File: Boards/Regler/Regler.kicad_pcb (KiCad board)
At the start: 2 copper layers, 21 parts, among them P1 CONN_2, P2 CONN_3, P3 CONN_3, P4 CONN_3, P5 CONN_3, P6 CONN_3, SW1 SP3T

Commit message: Anoden-Stabi auf eigenes Board, Endstufe Layouttest
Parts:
- RL1, RL2, RL3: footprint w_relay:relay_40.52 -> Relays_ThroughHole:Relay_DPDT_Schrack-RT2_RM5mm
- moved P6 54.8 mm to (130.0, 94.5)
- moved RL1 46.0 mm to (183.4, 113.3)
- moved D1 41.4 mm to (179.8, 120.4)
- moved P2 34.5 mm to (195.1, 94.5)
- moved RL2 29.8 mm to (148.8, 113.3)
- moved D6 27.9 mm to (195.6, 137.7)
- moved R3 27.0 mm to (198.1, 126.5), turned to 270 degrees
- moved D3 23.5 mm to (144.8, 120.4), turned to 180 degrees
- moved D2 18.2 mm to (215.4, 137.7)
- moved RL3 18.1 mm to (118.4, 113.8)
- moved R2 13.5 mm to (208.8, 126.5), turned to 270 degrees
- moved D4 12.2 mm to (206.2, 137.7)
- moved D5 11.4 mm to (114.8, 120.4), turned to 180 degrees
- moved P3 11.0 mm to (162.6, 94.5)
- moved RV1 10.8 mm to (83.3, 137.2)
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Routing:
- net Earth_Clean: track 25.0 -> 188.3 mm
- net Net-(P3-Pad1): track 136.3 -> 22.4 mm
- net +12V: track 85.8 -> 0.00 mm
- net Net-(P6-Pad1): track 79.1 -> 20.6 mm
- net Net-(D1-Pad1): track 137.1 -> 82.0 mm
- net Net-(RL1-Pad24): track 47.3 -> 0.00 mm
- net Net-(D5-Pad1): track 203.8 -> 159.2 mm
- net Net-(RL1-Pad14): track 41.0 -> 0.00 mm
- net GND: track 0.00 -> 36.1 mm
- net Net-(P6-Pad3): track 41.4 -> 13.8 mm
- net Net-(D3-Pad1): track 141.3 -> 117.4 mm
- net Net-(P2-Pad3): track 28.3 -> 14.0 mm
- net Net-(P3-Pad3): track 29.8 -> 16.1 mm
- net Net-(D6-Pad2): track 3.81 -> 6.10 mm
- net Net-(D4-Pad2): track 3.81 -> 6.10 mm
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- added copper zone on B.Cu, net GND
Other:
- net class Default: trace_width 0.5 -> 1

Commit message: Work in Progress
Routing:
- net Net-(RL1-Pad24): track 0.00 -> 69.7 mm
- net Net-(RL1-Pad14): track 0.00 -> 69.7 mm
- net +12V: track 0.00 -> 49.4 mm, vias 0 -> 2
- net Net-(D3-Pad1): track 117.4 -> 122.6 mm
- net Earth_Clean: track 188.3 -> 186.8 mm
- net Net-(D1-Pad1): track 82.0 -> 80.5 mm

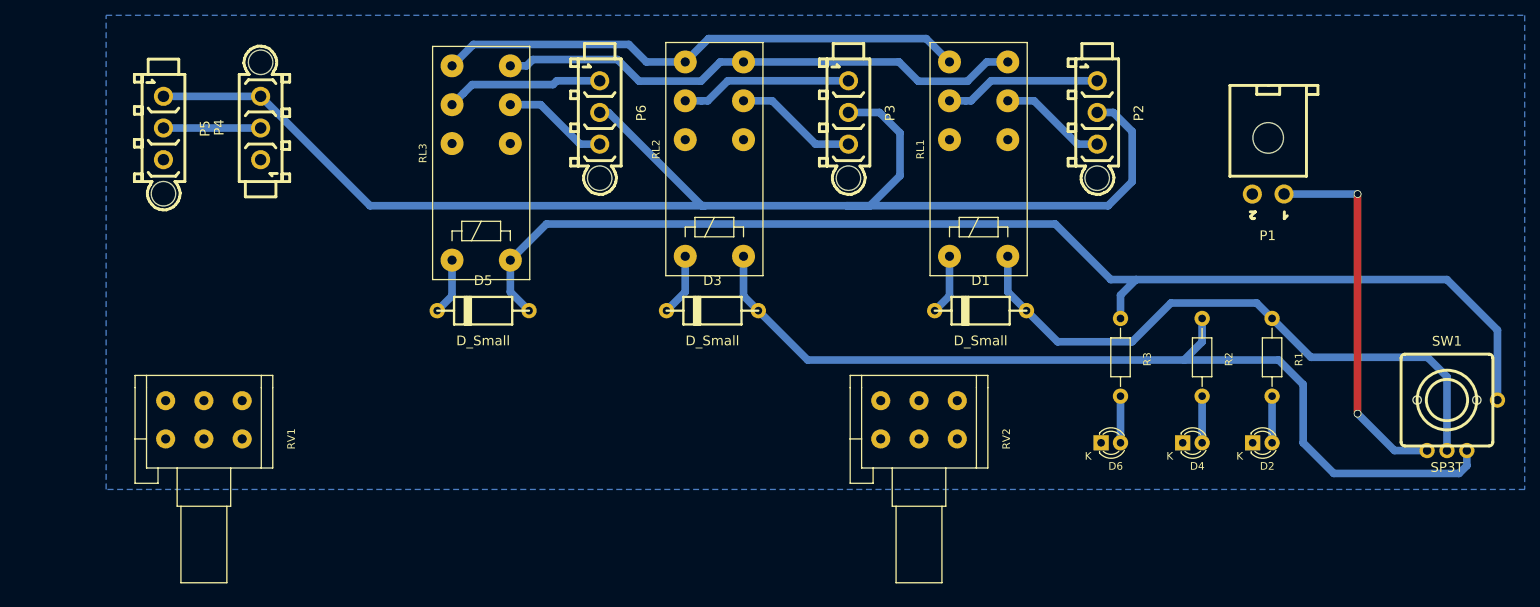
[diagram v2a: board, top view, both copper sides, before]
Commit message: New Potis
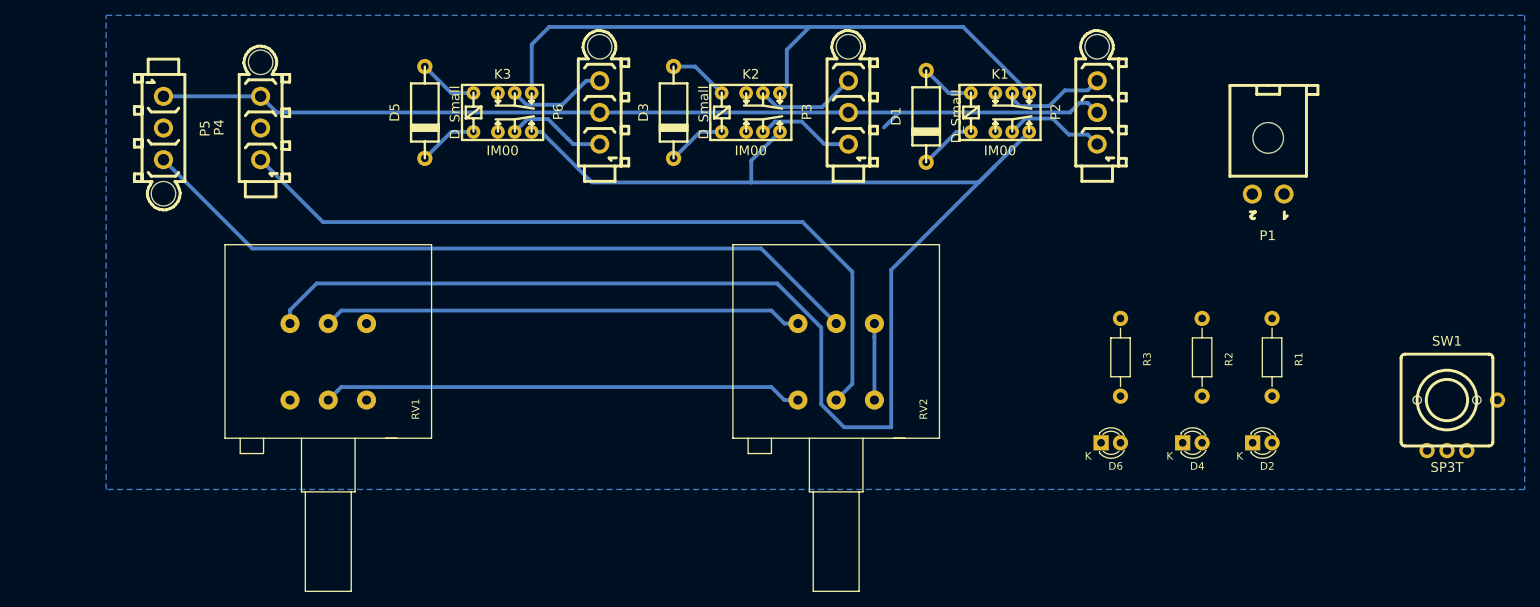
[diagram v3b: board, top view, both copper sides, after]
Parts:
- removed RL1, RL2, RL3: FINDER-30.22, Relays_ThroughHole:Relay_DPDT_Schrack-RT2_RM5mm
- added K1: IM00, w_relay:relay_gq-pth, F.Cu at (182.4, 94.5)
- added K2: IM00, w_relay:relay_gq-pth, F.Cu at (149.8, 94.5)
- added K3: IM00, w_relay:relay_gq-pth, F.Cu at (117.3, 94.5)
- RV1, RV2: footprint Potentiometers:Potentiometer_Alps-RK16-double -> Potentiometer_Alps_RKxxx:Potentiometer_Alps-RK271-double
- moved D5 27.0 mm to (107.2, 94.5), turned to 270 degrees
- moved D3 26.4 mm to (139.7, 94.5), turned to 270 degrees
- moved D1 26.4 mm to (172.7, 95.0), turned to 270 degrees
- moved RV1 16.7 mm to (99.6, 133.3)
- moved RV2 11.5 mm to (166.0, 133.3)
- turned P2 to 90 degrees
- turned P3 to 90 degrees
- turned P6 to 90 degrees
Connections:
- P4 pad 1: (no net) -> Net-(P4-Pad1)
- P5 pad 3: (no net) -> Net-(P5-Pad3)
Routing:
- net Net-(K1-Pad4): track 0.00 -> 213.7 mm
- net Net-(D5-Pad1): track 159.4 -> 7.78 mm
- net Net-(D3-Pad1): track 122.6 -> 7.72 mm
- net Net-(P4-Pad1): track 0.00 -> 101.1 mm
- net Net-(P5-Pad3): track 0.00 -> 96.8 mm
- net Net-(K1-Pad5): track 0.00 -> 86.1 mm
- net Net-(D1-Pad1): track 80.5 -> 7.06 mm
- net Net-(RL1-Pad24): track 69.7 -> 0.00 mm
- net Net-(RL1-Pad14): track 69.7 -> 0.00 mm
- net Net-(RV1-Pad2): track 0.00 -> 62.8 mm
- net Net-(RV1-Pad5): track 0.00 -> 62.8 mm
- net Earth_Clean: track 186.8 -> 136.7 mm
- net +12V: track 49.4 -> 0.00 mm, vias 2 -> 0
- net GND: track 36.1 -> 23.0 mm
- net Net-(K2-Pad3): track 22.4 -> 13.0 mm
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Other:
- net class Default: trace_width 1 -> 0.5; via_dia 1 -> 1.6

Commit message: Work in Progress
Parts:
- removed D1, D3, D5: D_Small, w_pth_diodes:diode_do15
- removed D2, D4, D6: LED, LEDs:LED-3MM
- removed K1, K2, K3: IM00, w_relay:relay_gq-pth
- removed P4, P5, P6: CONN_3, MiniUniversalMate-N-LokSockets_13Aug2012:MiniUniversalMate-N-LokSocket_3PinVertical_12Aug2012
- removed R1, R2, R3: R, Resistors_ThroughHole:Resistor_Horizontal_RM10mm
- removed SW1: SP3T, w_switch:pcb_push_xiejia_pb-11d14
- added REF**: EuroBoard_halb_Type-II_160mmX50mm_holes, EuroBoard_Outline:EuroBoard_halb_Type-II_160mmX50mm_holes, F.Cu at (53.8, 137.7)
- P1: value CONN_2 -> CONN_3; footprint MiniUniversalMate-N-LokSockets_13Aug2012:MiniUniversalMate-N-LokSocket_2PinHorizontal_13Aug2012 -> Sockets_Mini-Universal:MiniUniversalMate-N-LokSocket_3PinVertical
- P2, P3: value CONN_3 -> CONN_2; footprint MiniUniversalMate-N-LokSockets_13Aug2012:MiniUniversalMate-N-LokSocket_3PinVertical_12Aug2012 -> Sockets_Mini-Universal:MiniUniversalMate-N-LokSocket_2PinVertical
- moved RV1 93.9 mm to (193.5, 133.3)
- moved RV2 77.1 mm to (88.8, 133.3)
- moved P1 63.3 mm to (154.3, 110.5), turned to 90 degrees
- moved P2 62.5 mm to (134.6, 110.3), turned to 270 degrees
- moved P3 44.0 mm to (121.3, 109.9), turned to 270 degrees
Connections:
- P1 pad 1: +12V -> Net-(P1-Pad1)
- P1 pad 2: GND -> Earth_Clean
- P2 pad 1: Net-(K1-Pad3) -> Net-(P2-Pad1)
- P3 pad 1: Net-(K2-Pad3) -> Net-(P3-Pad1)
- RV1 pad 1: (no net) -> Earth_Clean
- RV1 pad 3: Net-(K1-Pad5) -> Net-(P1-Pad1)
- RV1 pad 4: Net-(K1-Pad4) -> Net-(P1-Pad3)
- RV1 pad 6: (no net) -> Earth_Clean
- RV2 pad 2: Net-(P4-Pad1) -> Net-(P2-Pad1)
- RV2 pad 5: Net-(P5-Pad3) -> Net-(P3-Pad1)
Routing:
- net Net-(K1-Pad4): track 213.7 -> 0.00 mm
- net Net-(P4-Pad1): track 101.1 -> 0.00 mm
- net Net-(P5-Pad3): track 96.8 -> 0.00 mm
- net Net-(K1-Pad5): track 86.1 -> 0.00 mm
- net Net-(P2-Pad1): track 0.00 -> 79.8 mm
- net Net-(RV1-Pad5): track 62.8 -> 139.1 mm
- net Net-(RV1-Pad2): track 62.8 -> 113.4 mm
- net Net-(P1-Pad1): track 0.00 -> 48.9 mm
- net Earth_Clean: track 136.7 -> 185.3 mm
- net Net-(P3-Pad1): track 0.00 -> 46.3 mm
- net Net-(P1-Pad3): track 0.00 -> 39.1 mm
- net GND: track 23.0 -> 0.00 mm
- net Net-(K1-Pad6): track 13.6 -> 0.00 mm
- net Net-(K2-Pad6): track 13.4 -> 0.00 mm
- net Net-(K1-Pad3): track 13.2 -> 0.00 mm
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- removed copper zone on B.Cu, net GND
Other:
- board outline added: 160 x 50 mm
- net class Default: trace_width 0.5 -> 1; via_dia 1.6 -> 2; via_drill 0.8 -> 1

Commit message: Work in Progress
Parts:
- P1: footprint Sockets_Mini-Universal:MiniUniversalMate-N-LokSocket_3PinVertical -> Connectors_Molex:Molex_KK-6410-03_03x2.54mm_Straight
- P2, P3: footprint Sockets_Mini-Universal:MiniUniversalMate-N-LokSocket_2PinVertical -> Connectors_Molex:Molex_KK-6410-02_02x2.54mm_Straight
- moved P2 0.47 mm to (134.6, 109.9)
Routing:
- net Net-(RV1-Pad5): track 139.1 -> 131.5 mm
- net Net-(P2-Pad1): track 79.8 -> 76.0 mm
- net Net-(P1-Pad3): track 39.1 -> 36.1 mm
- net Earth_Clean: track 185.3 -> 182.4 mm
- net Net-(RV1-Pad2): track 113.4 -> 112.4 mm
- net Net-(P3-Pad1): track 46.3 -> 45.5 mm
- net Net-(P1-Pad1): track 48.9 -> 48.2 mm

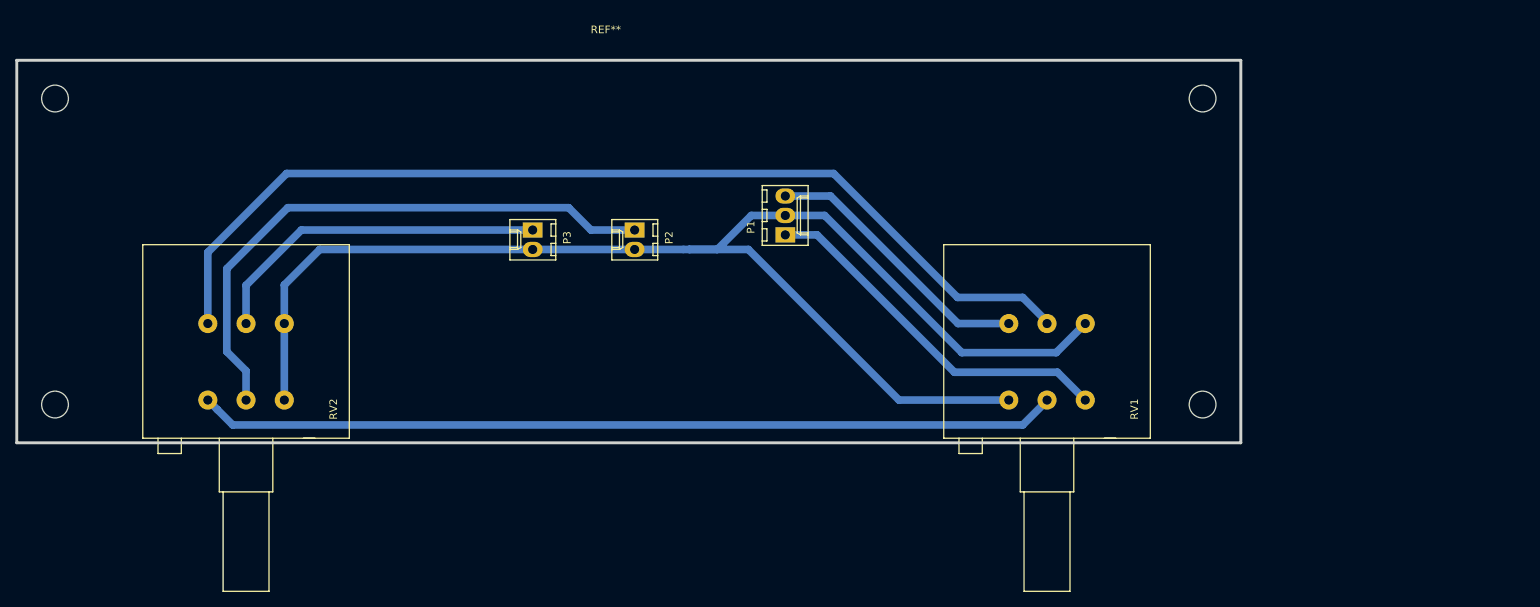
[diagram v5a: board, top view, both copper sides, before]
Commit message: Converted to Kicad 5.1 and Layout changes
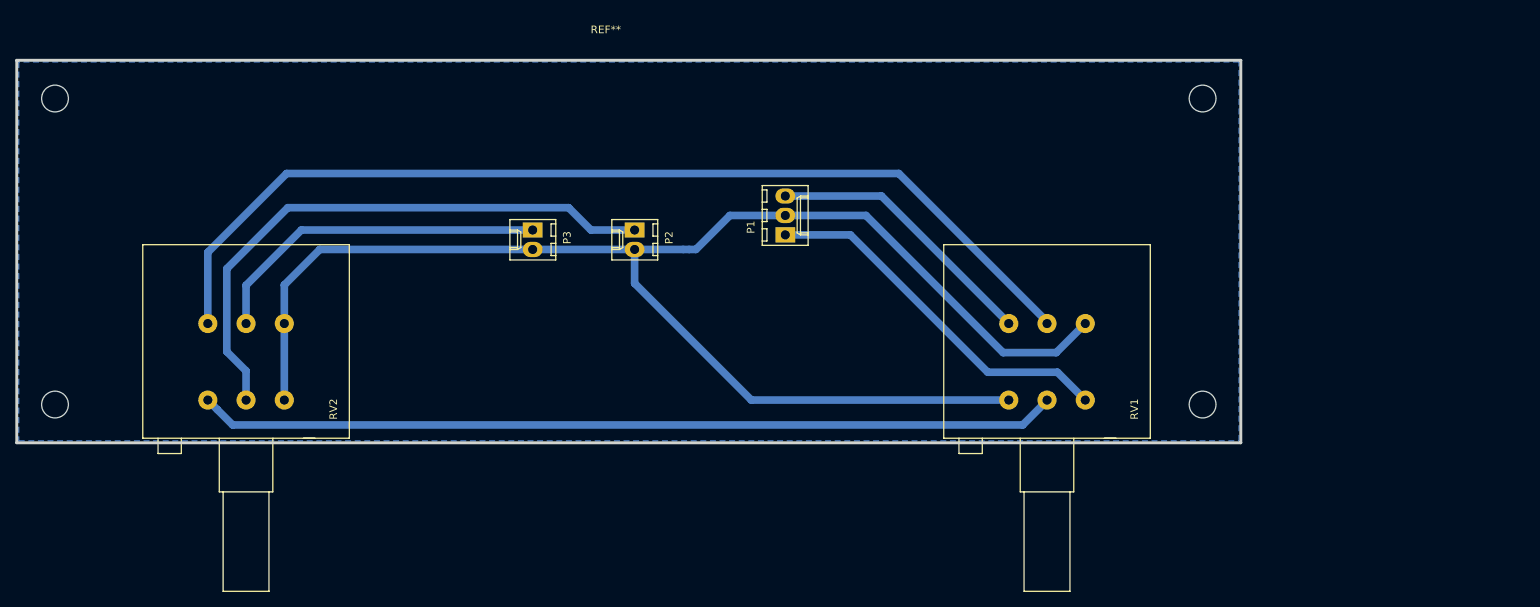
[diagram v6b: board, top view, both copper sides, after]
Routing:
- net Earth_Clean: track 182.4 -> 192.2 mm
- added copper zone on B.Cu, net Earth_Clean
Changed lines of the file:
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@@
-(kicad_pcb (version 20171130) (host pcbnew "(5.0.0)")
+(kicad_pcb (version 20171130) (host pcbnew "(5.1.0)-1")
   (general
     (thickness 1.6)
     (drawings 0)
-    (tracks 46)
+    (tracks 44)
     (zones 0)
     (modules 6)
@@
     (zone_45_only no)
     (trace_min 0.2)
-    (segment_width 0.2)
-    (edge_width 0.15)
     (via_size 2)
     (via_drill 1)
@@
     (uvia_min_size 0.2)
     (uvia_min_drill 0.1)
+    (edge_width 0.15)
+    (segment_width 0.2)
     (pcb_text_width 0.3)
     (pcb_text_size 1.5 1.5)
@@
     )
   )
-  (segment (start 193.515 122.08) (end 189.714232 125.880768) (width 1) (layer B.Cu) (net 1))
-  (segment (start 159.449051 107.95) (end 154.305 107.95) (width 1) (layer B.Cu) (net 1))
-  (segment (start 189.714232 125.880768) (end 177.379819 125.880768) (width 1) (layer B.Cu) (net 1))
-  (segment (start 177.379819 125.880768) (end 159.449051 107.95) (width 1) (layer B.Cu) (net 1))
-  (segment (start 183.515 132.08) (end 169.166226 132.08) (width 1) (layer B.Cu) (net 1))
-  (segment (start 169.166226 132.08) (end 149.481226 112.395) (width 1) (layer B.Cu) (net 1))
-  (segment (start 149.481226 112.395) (end 141.732 112.395) (width 1) (layer B.Cu) (net 1))
   (segment (start 140.97 112.395) (end 141.732 112.395) (width 1) (layer B.Cu) (net 1))
   (segment (start 134.60984 112.395) (end 140.97 112.395) (width 1) (layer B.Cu) (net 1))
@@
   (segment (start 88.82 117.035569) (end 88.82 122.08) (width 1) (layer B.Cu) (net 1))
   (segment (start 88.82 132.08) (end 88.82 122.08) (width 1) (layer B.Cu) (net 1))
-  (segment (start 145.415 112.395) (end 141.732 112.395) (width 1) (layer B.Cu) (net 1))
-  (segment (start 154.305 107.95) (end 149.86 107.95) (width 1) (layer B.Cu) (net 1))
-  (segment (start 149.86 107.95) (end 145.415 112.395) (width 1) (layer B.Cu) (net 1))
+  (segment (start 142.621 112.395) (end 141.732 112.395) (width 1) (layer B.Cu) (net 1))
+  (segment (start 154.305 107.95) (end 147.066 107.95) (width 1) (layer B.Cu) (net 1))
+  (segment (start 147.066 107.95) (end 142.621 112.395) (width 1) (layer B.Cu) (net 1))
+  (segment (start 134.60984 116.82984) (end 134.60984 112.395) (width 1) (layer B.Cu) (net 1))
+  (segment (start 183.515 132.08) (end 149.86 132.08) (width 1) (layer B.Cu) (net 1))
+  (segment (start 149.86 132.08) (end 134.60984 116.82984) (width 1) (layer B.Cu) (net 1))
+  (segment (start 164.846 107.95) (end 154.305 107.95) (width 1) (layer B.Cu) (net 1))
+  (segment (start 182.776768 125.880768) (end 164.846 107.95) (width 1) (layer B.Cu) (net 1))
+  (segment (start 193.515 122.08) (end 189.714232 125.880768) (width 1) (layer B.Cu) (net 1))
+  (segment (start 189.714232 125.880768) (end 182.776768 125.880768) (width 1) (layer B.Cu) (net 1))
   (segment (start 78.82 112.768719) (end 78.82 122.08) (width 1) (layer B.Cu) (net 2))
-  (segment (start 188.515 121.84) (end 185.341904 118.666904) (width 1) (layer B.Cu) (net 2))
-  (segment (start 185.341904 118.666904) (end 176.823253 118.666904) (width 1) (layer B.Cu) (net 2))
-  (segment (start 176.823253 118.666904) (end 160.6227 102.466351) (width 1) (layer B.Cu) (net 2))
+  (segment (start 89.122368 102.466351) (end 78.82 112.768719) (width 1) (layer B.Cu) (net 2))
+  (segment (start 169.141351 102.466351) (end 89.122368 102.466351) (width 1) (layer B.Cu) (net 2))
   (segment (start 188.515 122.08) (end 188.515 121.84) (width 1) (layer B.Cu) (net 2))
-  (segment (start 160.6227 102.466351) (end 89.122368 102.466351) (width 1) (layer B.Cu) (net 2))
-  (segment (start 89.122368 102.466351) (end 78.82 112.768719) (width 1) (layer B.Cu) (net 2))
+  (segment (start 188.515 121.84) (end 169.141351 102.466351) (width 1) (layer B.Cu) (net 2))
   (segment (start 80.069679 133.329679) (end 78.82 132.08) (width 1) (layer B.Cu) (net 3))
   (segment (start 82.073896 135.333896) (end 80.069679 133.329679) (width 1) (layer B.Cu) (net 3))
@@
   (segment (start 188.515 132.08) (end 188.515 132.16) (width 1) (layer B.Cu) (net 3))
   (segment (start 188.515 132.16) (end 185.341104 135.333896) (width 1) (layer B.Cu) (net 3))
+  (segment (start 162.814 110.49) (end 154.305 110.49) (width 1) (layer B.Cu) (net 4))
+  (segment (start 180.768734 128.444734) (end 162.814 110.49) (width 1) (layer B.Cu) (net 4))
   (segment (start 193.515 132.08) (end 189.879734 128.444734) (width 1) (layer B.Cu) (net 4))
-  (segment (start 189.879734 128.444734) (end 176.411341 128.444734) (width 1) (layer B.Cu) (net 4))
-  (segment (start 176.411341 128.444734) (end 158.456607 110.49) (width 1) (layer B.Cu) (net 4))
-  (segment (start 158.456607 110.49) (end 154.305 110.49) (width 1) (layer B.Cu) (net 4))
-  (segment (start 154.305 105.41) (end 160.215056 105.41) (width 1) (layer B.Cu) (net 5))
-  (segment (start 160.215056 105.41) (end 176.885056 122.08) (width 1) (layer B.Cu) (net 5))
-  (segment (start 176.885056 122.08) (end 183.515 122.08) (width 1) (layer B.Cu) (net 5))
+  (segment (start 189.879734 128.444734) (end 180.768734 128.444734) (width 1) (layer B.Cu) (net 4))
+  (segment (start 183.515 122.047) (end 183.515 122.08) (width 1) (layer B.Cu) (net 5))
+  (segment (start 154.305 105.41) (end 166.878 105.41) (width 1) (layer B.Cu) (net 5))
+  (segment (start 166.878 105.41) (end 183.515 122.047) (width 1) (layer B.Cu) (net 5))
   (segment (start 128.905 109.855) (end 125.984963 106.934963) (width 1) (layer B.Cu) (net 6))
   (segment (start 83.82 128.27) (end 83.82 132.08) (width 1) (layer B.Cu) (net 6))
@@
   (segment (start 121.285 109.855) (end 91.045972 109.855) (width 1) (layer B.Cu) (net 7))
   (segment (start 83.82 117.080972) (end 83.82 122.08) (width 1) (layer B.Cu) (net 7))
+  (zone (net 1) (net_name Earth_Clean) (layer B.Cu) (hatch edge 0.508)
+    (connect_pads (clearance 0.508))
+    (min_thickness 0.254)
+    (fill yes (arc_segments 32) (thermal_gap 0.508) (thermal_bridge_width 0.508))
+    (polygon
+      (pts
+        (xy 54.102 87.884) (xy 54.102 137.414) (xy 213.614 137.414) (xy 213.614 87.884)
+      )
+    )
+  )
 )

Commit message: Minor Layout changes
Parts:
- P1: value CONN_3 -> LV_In
- P2: value CONN_2 -> LV_Out_L
- P3: value CONN_2 -> LV_Out_R
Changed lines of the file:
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@@
       (effects (font (size 1 1) (thickness 0.15)))
     )
-    (fp_text value CONN_3 (at 2.54 4.5 90) (layer F.Fab)
+    (fp_text value LV_In (at 2.54 4.5 90) (layer F.Fab)
       (effects (font (size 1 1) (thickness 0.15)))
     )
@@
       (effects (font (size 1 1) (thickness 0.15)))
     )
-    (fp_text value CONN_2 (at 1.27 4.5 270) (layer F.Fab)
+    (fp_text value LV_Out_L (at 1.27 4.5 270) (layer F.Fab)
       (effects (font (size 1 1) (thickness 0.15)))
     )
@@
       (effects (font (size 1 1) (thickness 0.15)))
     )
-    (fp_text value CONN_2 (at 1.27 4.5 270) (layer F.Fab)
+    (fp_text value LV_Out_R (at 1.27 4.5 270) (layer F.Fab)
       (effects (font (size 1 1) (thickness 0.15)))
     )
